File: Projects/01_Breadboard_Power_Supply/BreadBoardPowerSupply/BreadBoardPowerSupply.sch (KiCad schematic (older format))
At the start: 15 parts, among them J1 Barrel_Jack_Switch, J2 Conn_02x02_Odd_Even, J3 Conn_02x02_Odd_Even, SW1 SW_DPDT_x2, U1 LM7805_TO220

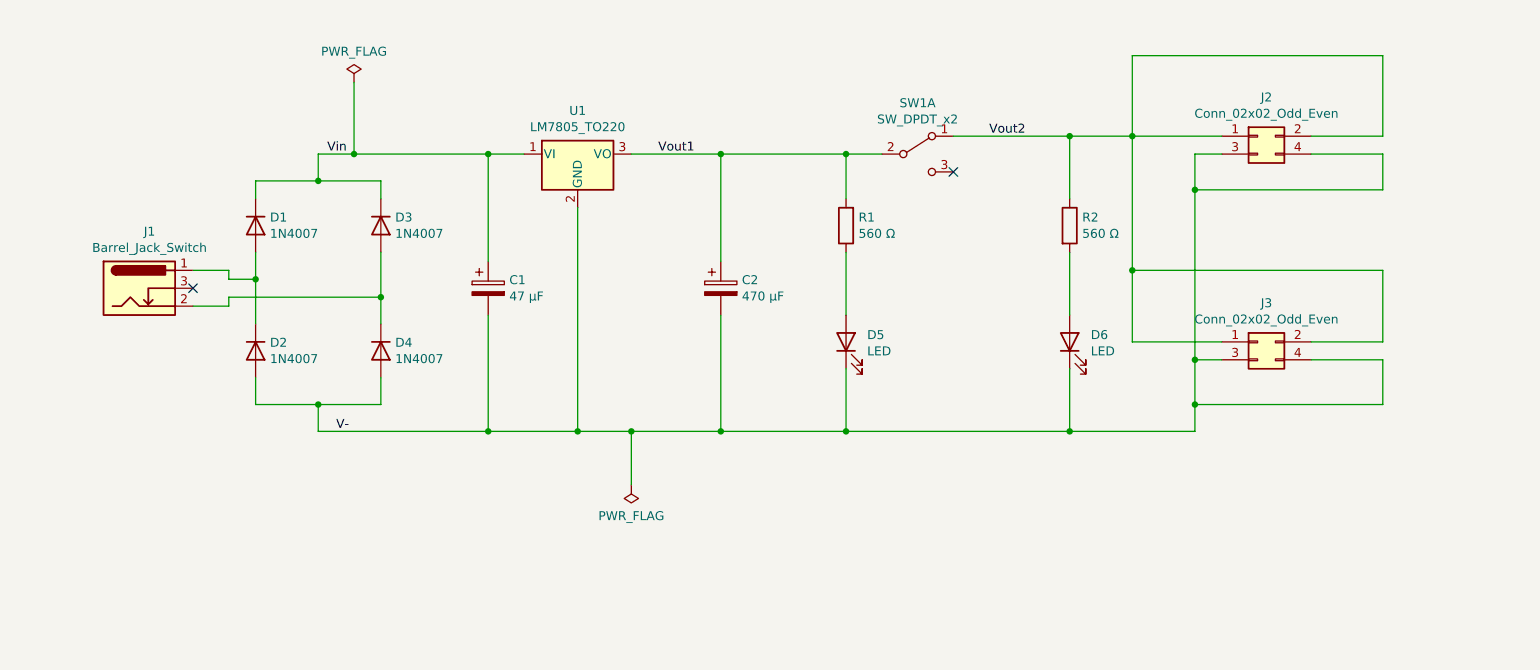
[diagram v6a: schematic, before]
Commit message: Add comments/text information about the circuit in the Eeschema
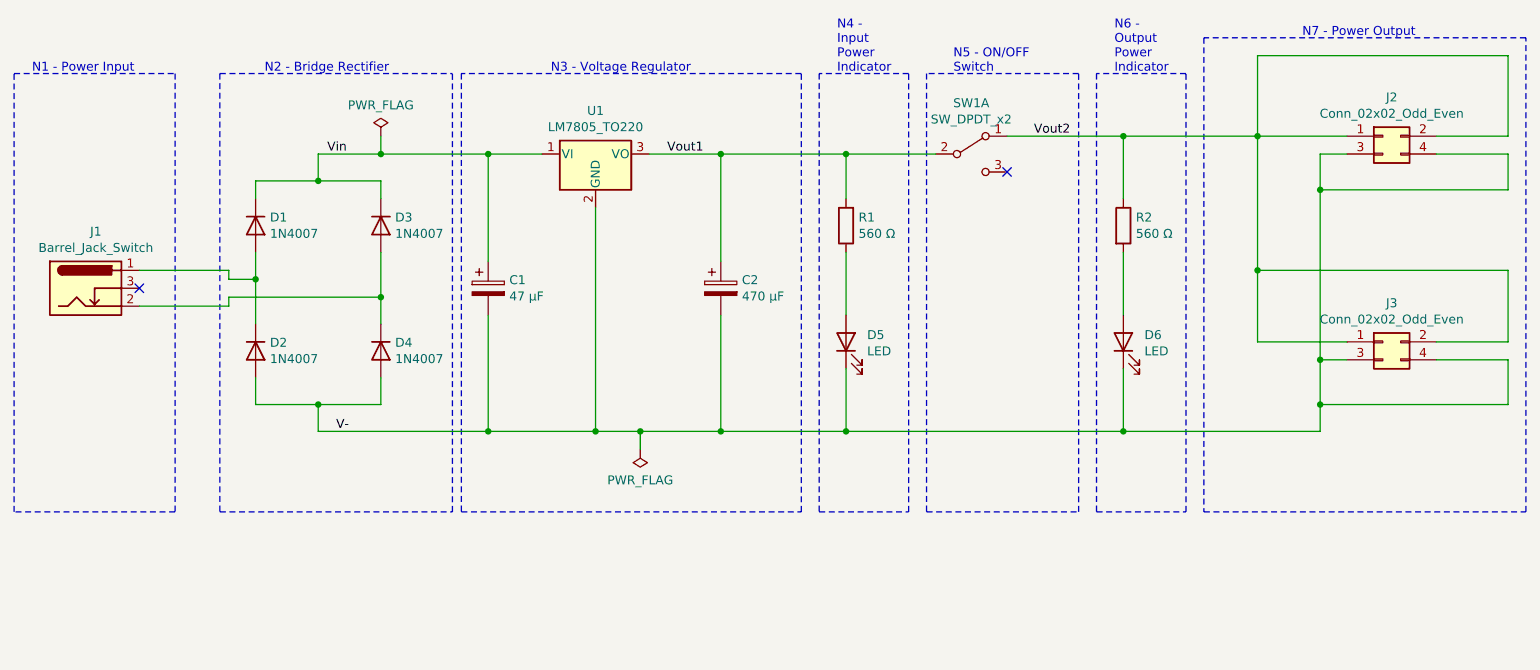
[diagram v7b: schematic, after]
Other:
- note added: "N1 - Power Input"
- note added: "N2 - Bridge Rectifier"
- note added: "N3 - Voltage Regulator"
- note added: "N4 -\nInput\nPower\nIndicator"
- note added: "N5 - ON/OFF\nSwitch"
- note added: "N6 -\nOutput\nPower\nIndicator"
- note added: "N7 - Power Output"
- moved on the sheet: D6, J1, J2, J3, R2, SW1A, U1

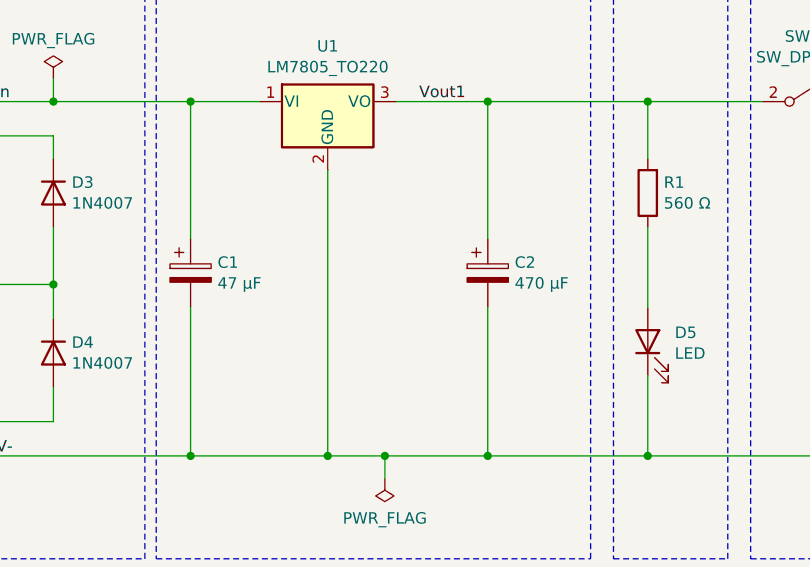
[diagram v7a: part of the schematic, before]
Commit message: Add silkscreen text and graphics: 	- Describe pads 	- Board version 	- Logos 	- Other Instructions 	- Added a PNG image of the 3=D PCB 	- Fixed Eeschema capacitors - C1 and C2 needed to their values 	  swapped
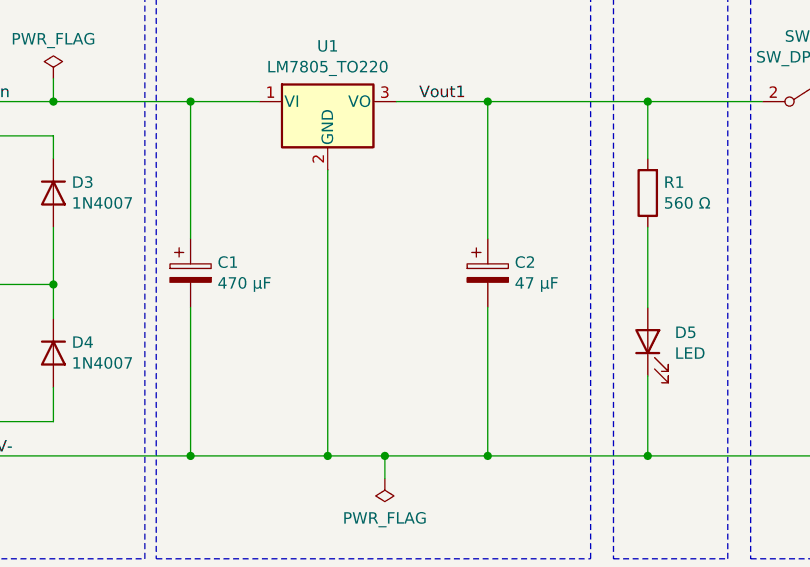
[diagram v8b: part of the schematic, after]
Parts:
- C1: value 47 μF -> 470 μF
- C2: value 470 μF -> 47 μF
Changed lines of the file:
@@
 P 5550 3350
 F 0 "C2" H 5668 3396 50  0000 L CNN
-F 1 "470 μF" H 5668 3305 50  0000 L CNN
+F 1 "47 μF" H 5668 3305 50  0000 L CNN
 F 2 "Capacitor_THT:CP_Radial_D6.3mm_P2.50mm" H 5588 3200 50  0001 C CNN
 F 3 "~" H 5550 3350 50  0001 C CNN
@@
 P 4250 3350
 F 0 "C1" H 4368 3396 50  0000 L CNN
-F 1 "47 μF" H 4368 3305 50  0000 L CNN
+F 1 "470 μF" H 4368 3305 50  0000 L CNN
 F 2 "Capacitor_THT:CP_Radial_D10.0mm_P5.00mm" H 4288 3200 50  0001 C CNN
 F 3 "~" H 4250 3350 50  0001 C CNN
